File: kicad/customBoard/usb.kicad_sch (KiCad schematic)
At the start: 28 parts

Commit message: Generate Netlist
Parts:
- C10, C11, C22, C23, C24, C25: renamed from C?; footprint Capacitor_SMD:C_0805_2012Metric -> Capacitor_SMD:C_1206_3216Metric_Pad1.33x1.80mm_HandSolder
- C12, C13, C14, C15, C16, C17, C20, C21: renamed from C?; footprint Capacitor_SMD:C_0402_1005Metric -> Capacitor_SMD:C_1206_3216Metric_Pad1.33x1.80mm_HandSolder
- C18, C19: renamed from C?; footprint (none) -> Capacitor_SMD:C_1206_3216Metric_Pad1.33x1.80mm_HandSolder
- C26: renamed from C?; footprint Capacitor_Tantalum_SMD:CP_EIA-7343-31_Kemet-D -> Capacitor_SMD:C_1206_3216Metric_Pad1.33x1.80mm_HandSolder
- J9: renamed from J?; footprint GCT_FFC3B07-20-T -> FFC3B07-20-T:GCT_FFC3B07-20-T
- R20, R21, R22, R23: renamed from R?; footprint Resistor_SMD:R_0402_1005Metric -> Resistor_SMD:R_1206_3216Metric_Pad1.30x1.75mm_HandSolder
- U9: renamed from U?; footprint SOT95P280X145-6N -> AP22653W6-7:SOT95P280X145-6N
- gave numbers to parts that had none: 5
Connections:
- net +3.3v renamed 3.3v

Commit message: First Draft of Power PCB
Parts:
- J6, J7, J8: footprint CONN15_2100-001_STW -> SS-52100-001:SS-52100-001
- U8: footprint TQFP64_10x10MC_MCH -> USB2504A-JT:USB2504A-JT
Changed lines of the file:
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@@
       (effects (font (size 1.524 1.524)) (justify left))
     )
-    (property "Footprint" "CONN15_2100-001_STW" (id 2) (at 234.95 109.474 0)
+    (property "Footprint" "SS-52100-001:SS-52100-001" (id 2) (at 234.95 109.474 0)
       (effects (font (size 1.524 1.524)) hide)
     )
@@
       (effects (font (size 1.524 1.524)) (justify left))
     )
-    (property "Footprint" "CONN15_2100-001_STW" (id 2) (at 234.95 132.334 0)
+    (property "Footprint" "SS-52100-001:SS-52100-001" (id 2) (at 234.95 132.334 0)
       (effects (font (size 1.524 1.524)) hide)
     )
@@
       (effects (font (size 1.524 1.524)) (justify left))
     )
-    (property "Footprint" "CONN15_2100-001_STW" (id 2) (at 234.95 155.194 0)
+    (property "Footprint" "SS-52100-001:SS-52100-001" (id 2) (at 234.95 155.194 0)
       (effects (font (size 1.524 1.524)) hide)
     )
@@
       (effects (font (size 1.524 1.524)))
     )
-    (property "Footprint" "TQFP64_10x10MC_MCH" (id 2) (at 92.71 24.384 0)
+    (property "Footprint" "USB2504A-JT:USB2504A-JT" (id 2) (at 92.71 24.384 0)
       (effects (font (size 1.524 1.524)) hide)
     )

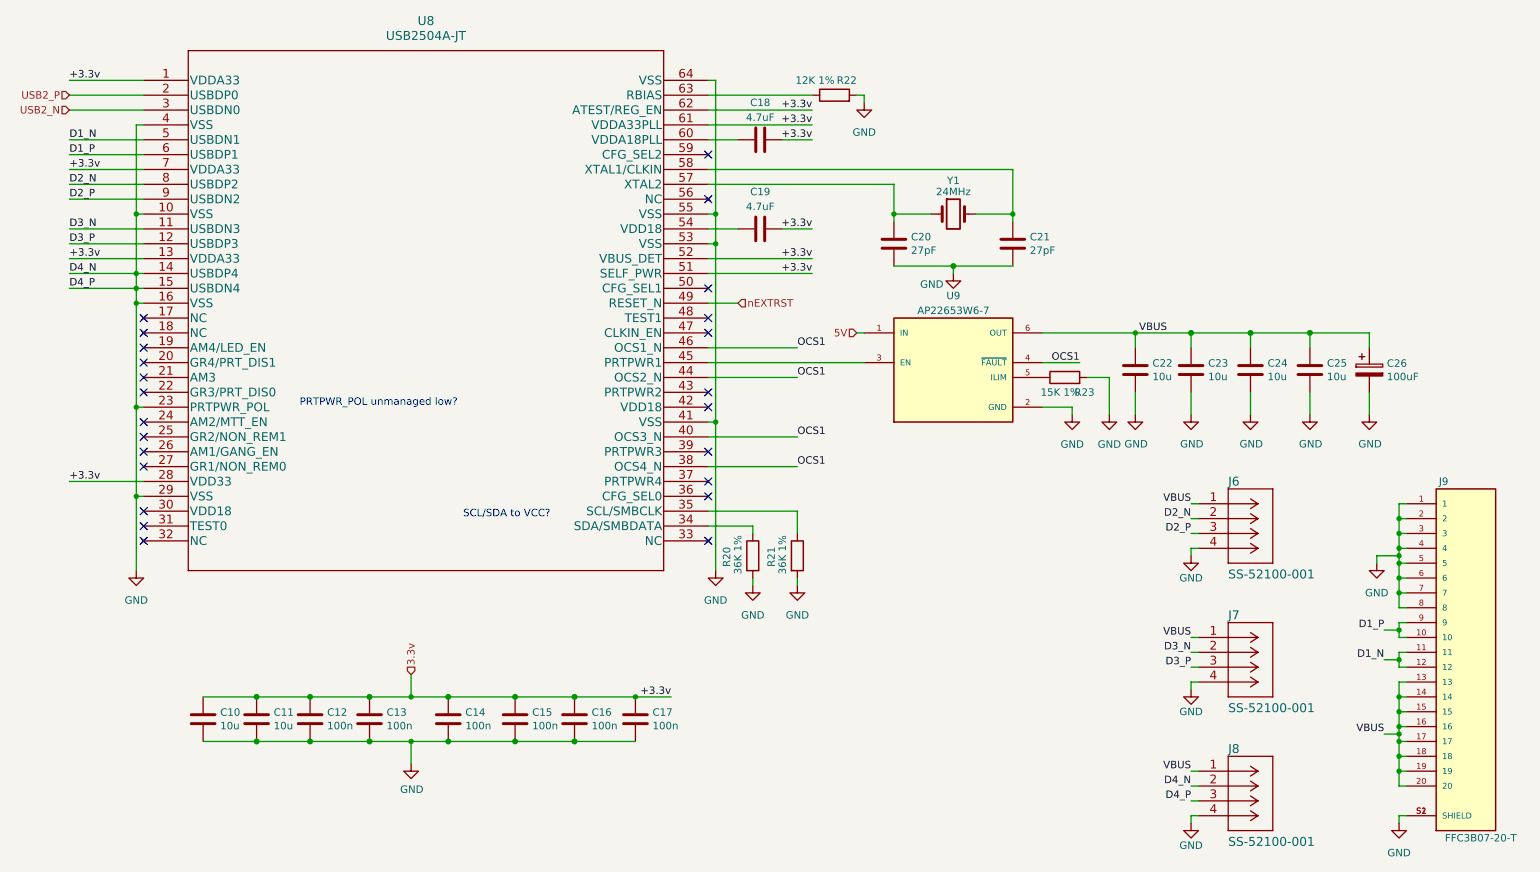
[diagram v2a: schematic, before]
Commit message: Rework Power PCB and draft SD
Moving things around so they would make sense on the final board. Flipped around some of the power circuit so the battery can be plugged in on the left side to make room for all the ports on the right.
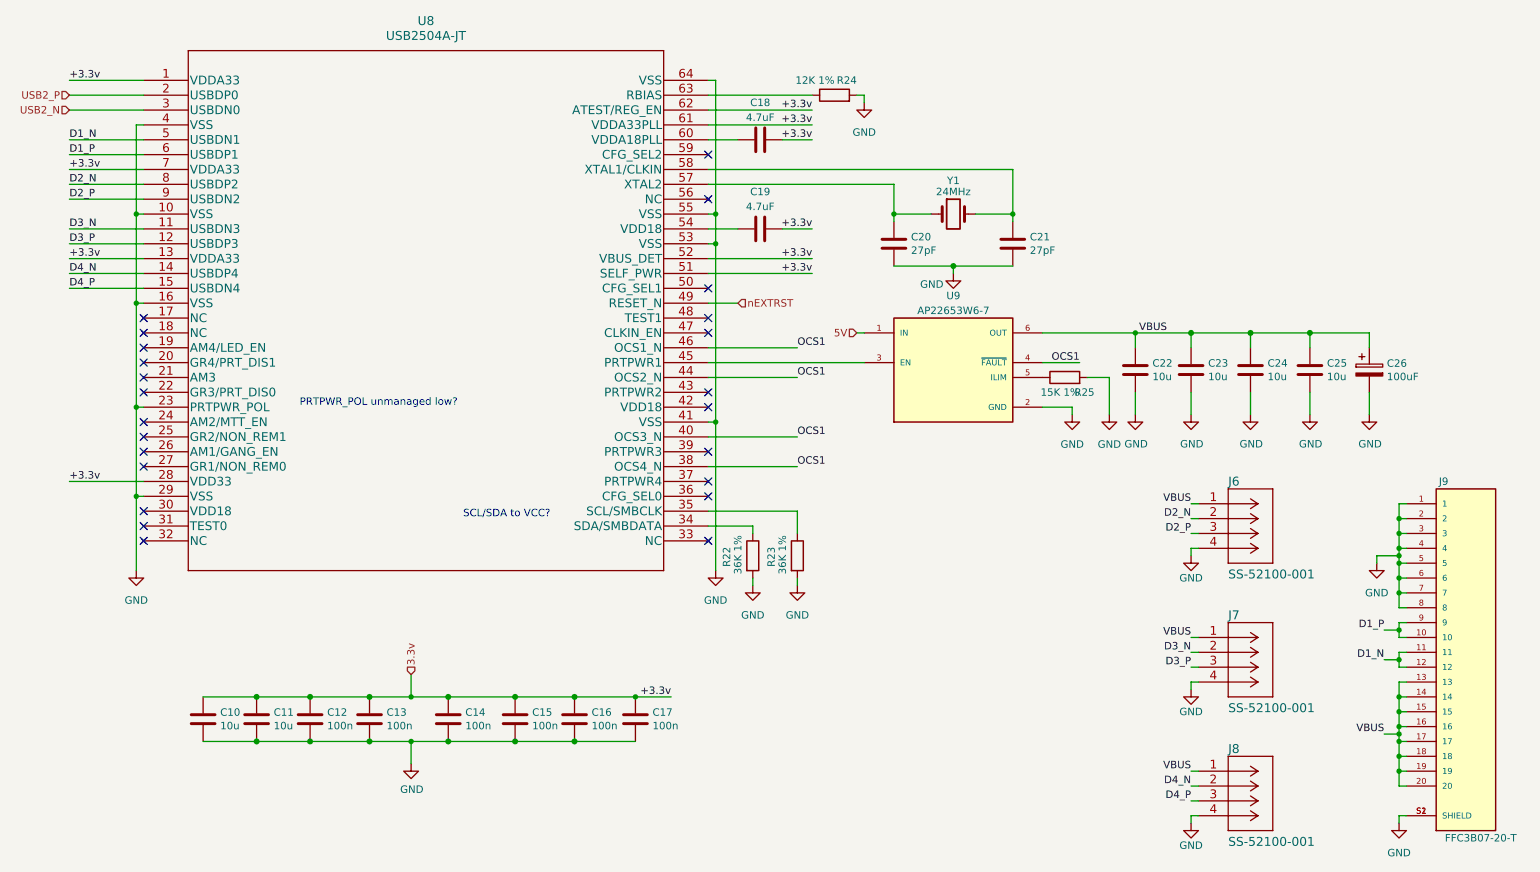
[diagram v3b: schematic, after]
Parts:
- renumbered R20 to R22, R21 to R23, R22 to R24, R23 to R25
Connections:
- net GND: no longer J8.2, J8.3, U8.14 (USBDP4), U8.15 (USBDN4)
- new net D4_N: J8.2, U8.14 (USBDP4)
- new net D4_P: J8.3, U8.15 (USBDN4)
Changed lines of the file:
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@@
   (paper "A4")
   (junction (at 43.18 53.34) (diameter 0.9144) (color 0 0 0 0))
-  (junction (at 43.18 63.5) (diameter 0.9144) (color 0 0 0 0))
-  (junction (at 43.18 66.04) (diameter 0.9144) (color 0 0 0 0))
   (junction (at 43.18 68.58) (diameter 0.9144) (color 0 0 0 0))
   (junction (at 43.18 86.36) (diameter 0.9144) (color 0 0 0 0))
@@
     (stroke (width 0) (type solid) (color 0 0 0 0))
   )
-  (wire (pts (xy 31.75 63.5) (xy 43.18 63.5))
-    (stroke (width 0) (type solid) (color 0 0 0 0))
-  )
-  (wire (pts (xy 31.75 66.04) (xy 43.18 66.04))
+  (wire (pts (xy 31.75 63.5) (xy 44.45 63.5))
+    (stroke (width 0) (type solid) (color 0 0 0 0))
+  )
+  (wire (pts (xy 31.75 66.04) (xy 44.45 66.04))
     (stroke (width 0) (type solid) (color 0 0 0 0))
   )
@@
     (stroke (width 0) (type solid) (color 0 0 0 0))
   )
+  (wire (pts (xy 43.18 53.34) (xy 43.18 68.58))
+    (stroke (width 0) (type solid) (color 0 0 0 0))
+  )
   (wire (pts (xy 43.18 53.34) (xy 44.45 53.34))
     (stroke (width 0) (type solid) (color 0 0 0 0))
   )
-  (wire (pts (xy 43.18 63.5) (xy 43.18 53.34))
-    (stroke (width 0) (type solid) (color 0 0 0 0))
-  )
-  (wire (pts (xy 43.18 66.04) (xy 43.18 63.5))
-    (stroke (width 0) (type solid) (color 0 0 0 0))
-  )
-  (wire (pts (xy 43.18 66.04) (xy 44.45 66.04))
-    (stroke (width 0) (type solid) (color 0 0 0 0))
-  )
-  (wire (pts (xy 43.18 68.58) (xy 43.18 66.04))
-    (stroke (width 0) (type solid) (color 0 0 0 0))
-  )
   (wire (pts (xy 43.18 68.58) (xy 44.45 68.58))
     (stroke (width 0) (type solid) (color 0 0 0 0))
@@
   )
   (wire (pts (xy 43.18 114.3) (xy 43.18 101.6))
-    (stroke (width 0) (type solid) (color 0 0 0 0))
-  )
-  (wire (pts (xy 44.45 63.5) (xy 43.18 63.5))
     (stroke (width 0) (type solid) (color 0 0 0 0))
   )
@@
   (symbol (lib_id "Device:R") (at 148.59 111.76 0) (unit 1)
     (in_bom yes) (on_board yes)
-    (property "Reference" "R20" (id 0) (at 144.145 113.665 90)
+    (property "Reference" "R22" (id 0) (at 144.145 113.665 90)
       (effects (font (size 1.27 1.27)) (justify left))
     )
@@
   (symbol (lib_id "Device:R") (at 156.21 111.76 0) (unit 1)
     (in_bom yes) (on_board yes)
-    (property "Reference" "R21" (id 0) (at 151.765 113.665 90)
+    (property "Reference" "R23" (id 0) (at 151.765 113.665 90)
       (effects (font (size 1.27 1.27)) (justify left))
     )
@@
   (symbol (lib_id "Device:R") (at 162.56 33.02 90) (unit 1)
     (in_bom yes) (on_board yes)
-    (property "Reference" "R22" (id 0) (at 166.37 30.48 90)
+    (property "Reference" "R24" (id 0) (at 166.37 30.48 90)
       (effects (font (size 1.27 1.27)) (justify left))
     )
@@
   (symbol (lib_id "Device:R") (at 201.93 81.28 90) (unit 1)
     (in_bom yes) (on_board yes)
-    (property "Reference" "R23" (id 0) (at 207.01 83.82 90)
+    (property "Reference" "R25" (id 0) (at 207.01 83.82 90)
       (effects (font (size 1.27 1.27)) (justify left))
     )

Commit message: Save progress on USB
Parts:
- removed C12, C13, C14: 100n, Capacitor_SMD:C_1206_3216Metric_Pad1.33x1.80mm_HandSolder, symbol Device:C
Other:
- moved on the sheet: C10, C11, C15, C16, C17

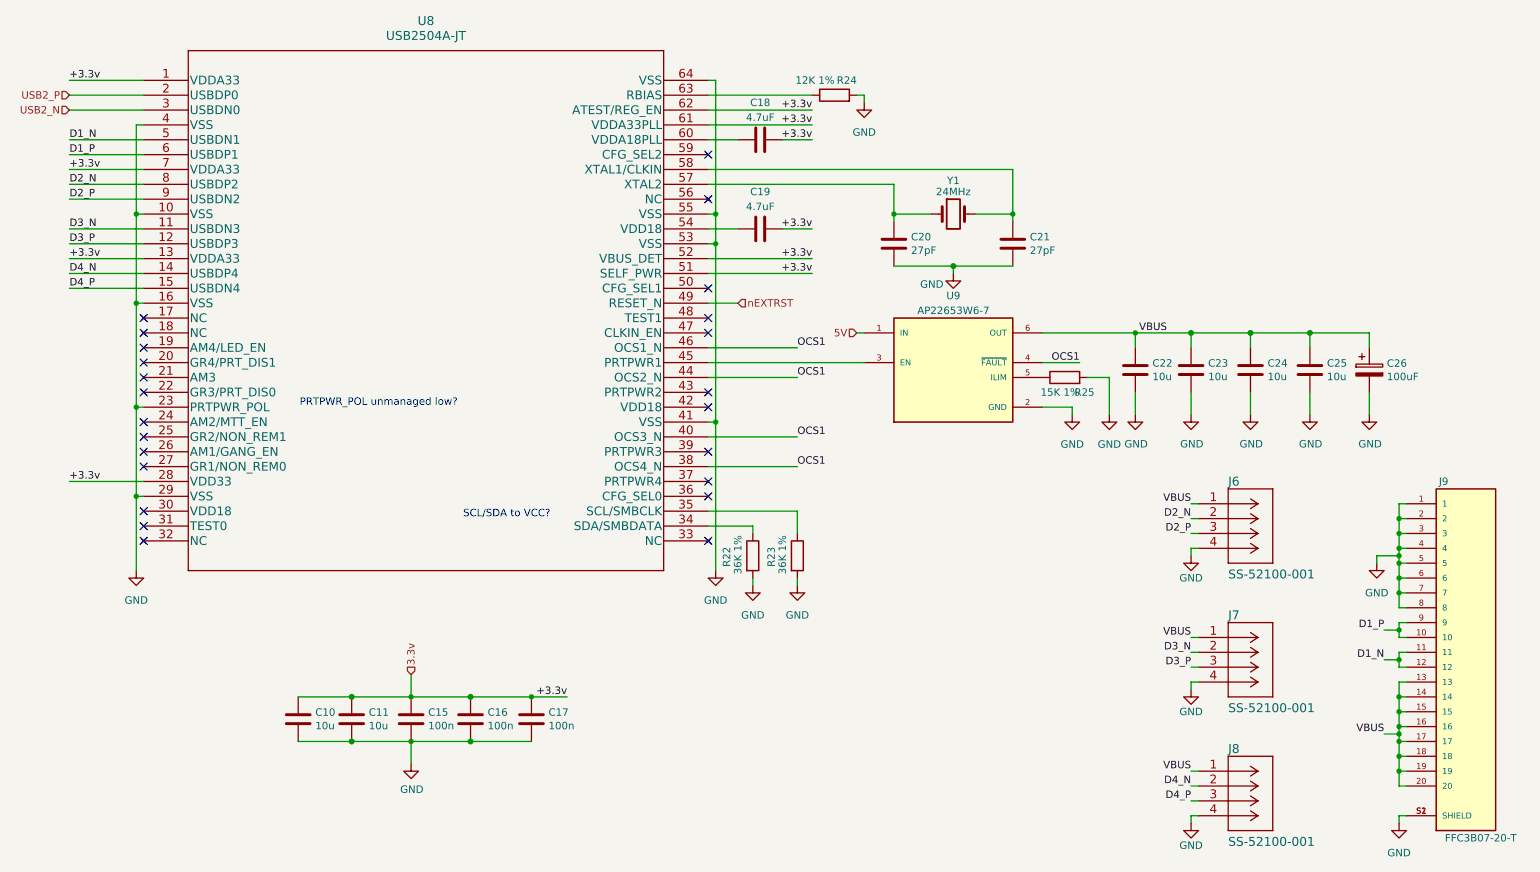
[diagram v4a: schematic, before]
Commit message: Draft HDMI and more differential pairs
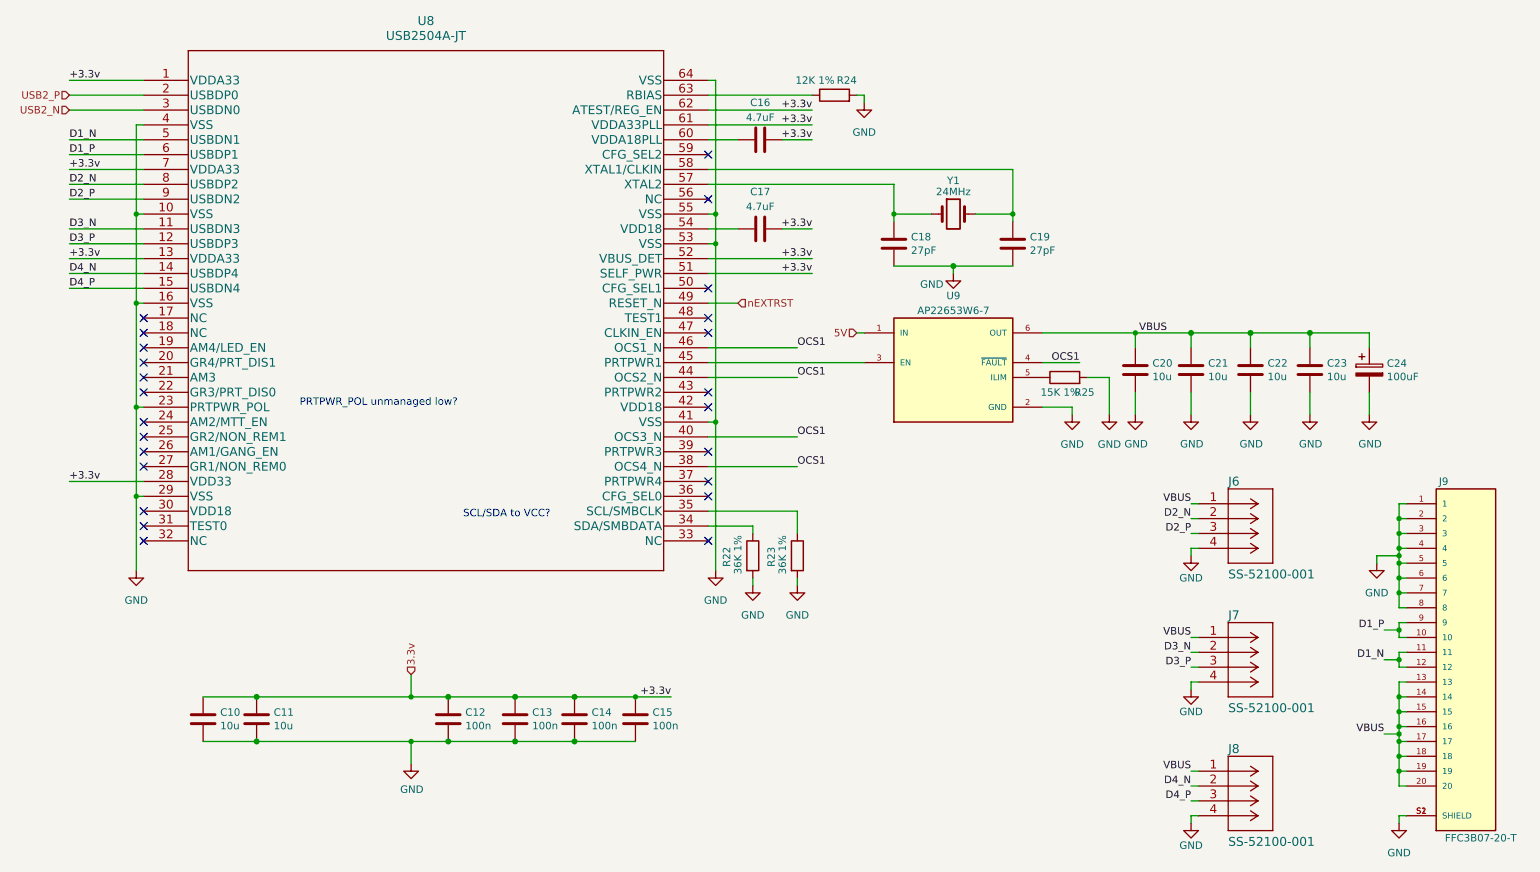
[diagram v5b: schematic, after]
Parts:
- added C12: 100n, Capacitor_SMD:C_1206_3216Metric_Pad1.33x1.80mm_HandSolder, symbol Device:C
- renumbered C15 to C13, C16 to C14, C17 to C15, C18 to C16, C19 to C17, C20 to C18, C21 to C19, C22 to C20, C23 to C21, C24 to C22, C25 to C23, C26 to C24
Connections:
- net 3.3v: now also C12.1
- net GND: now also C12.2
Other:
- moved on the sheet: C10, C11, C13, C14, C15

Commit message: Draft before fixing errors
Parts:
- removed C12: 100n, Capacitor_SMD:C_1206_3216Metric_Pad1.33x1.80mm_HandSolder, symbol Device:C
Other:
- moved on the sheet: C10, C11, C13, C14, C15

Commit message: Updates based on meeting with Dr. Jordan
Everything should be good to go now, next up is generating a bill of materials (making sure everything is in stock), and generating gerbers
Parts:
- added TP2: TestPoint, TestPoint:TestPoint_Pad_4.0x4.0mm, symbol Connector:TestPoint
- renumbered C13 to C12, C14 to C13, C15 to C14, C16 to C15, C17 to C16, C18 to C17, C19 to C18, C20 to C19, C21 to C20, C22 to C21, C23 to C22, C24 to C23, J9 to J10, J6 to J7, J7 to J8, J8 to J9
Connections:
- net GND: now also TP2.1

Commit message: Generate BOM
Clean up all the part data and add manufacturer's numbers for ordering
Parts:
- C10, C11, C19, C20, C21, C22: value 10u -> 10uF; Part Description 10uF 10% 10V Ceramic Capacitor X7R 0805 (2012 Metric) -> (none); manf# (none) -> CL31B106MOHNNNE
- C12, C13, C14: value 100n -> 0.1uF; Part Description 0.1uF 10% 16V Ceramic Capacitor X7R 0402 (1005 Metric) -> (none); manf# (none) -> CL31B104KBCNFNC
- C15, C16: manf# (none) -> CL31B475KAHNFNE
- C17, C18: Part Description 27pF 5% 50V Ceramic Capacitor C0G, NP0 0402 (1005 Metric) -> (none); manf# (none) -> C1206C270K5GAC7800
- C23: Part Description Capacitor, SP-Cap, 100u, 6.3V, 15mR ESR -> (none); manf# (none) -> GRM31CR60G107ME39L
- J10: MANUFACTURER GCT -> (none); MAXIMUM_PACKAGE_HEIGHT 2.5mm -> (none); PARTREV A -> (none); STANDARD Manufacturer Recommendations -> (none); manf# (none) -> FFC3B07-20-T
- J7, J8, J9: manf# (none) -> SS-52100-001
- R22, R23: Part Description Resistor 36K M1005 1% 63mW -> (none); manf# (none) -> RC1206FR-0736KL
- R24: Part Description Resistor 12K M1005 1% 63mW -> (none); manf# (none) -> RC1206FR-0712KL
- R25: Part Description Resistor 15K M1005 1% 63mW -> (none); manf# (none) -> RC1206FR-0715KL
- U8: manf# (none) -> USB2504A-JT
- U9: MANUFACTURER Diodes Inc. -> (none); MAXIMUM_PACKAGE_HEIGHT 1.45 mm -> (none); PARTREV 2-2 -> (none); STANDARD IPC 7351B -> (none); manf# (none) -> AP22653W6-7
- Y1: Part Description 24MHz Crystal 18pf 30ppm 30ppm -> (none); manf# (none) -> FC4SDCBMF24.0-T1
